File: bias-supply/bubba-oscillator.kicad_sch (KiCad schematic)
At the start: 14 parts, among them U1 MAX44243ASD+

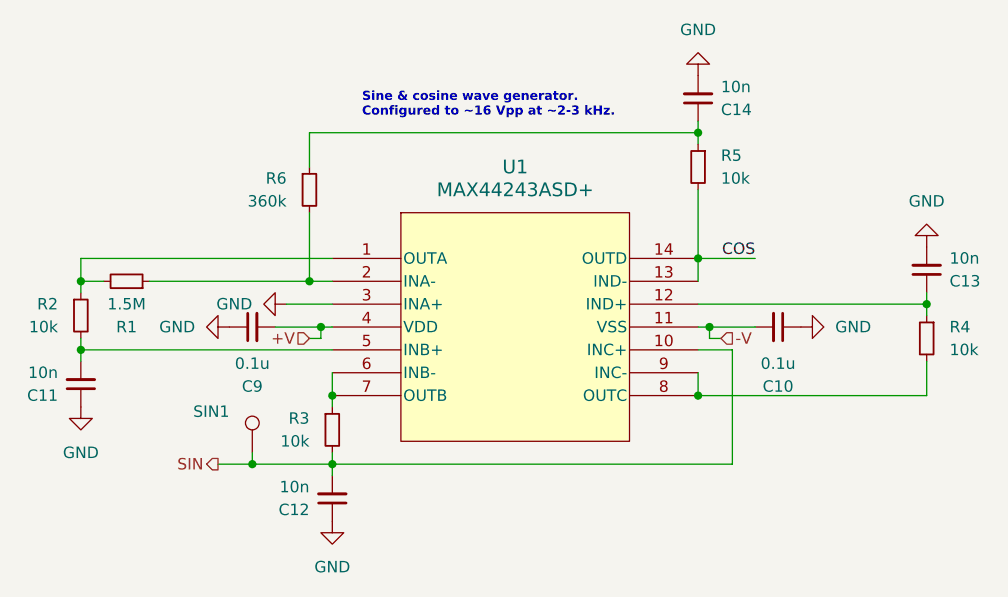
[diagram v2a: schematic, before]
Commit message: Add fuses; change to coax; fixed I2C gnd
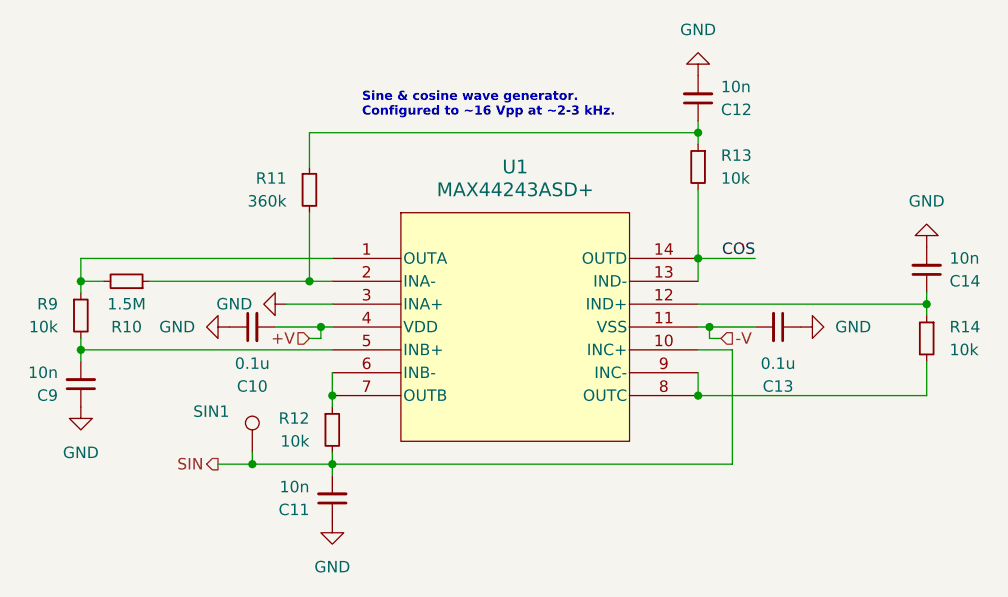
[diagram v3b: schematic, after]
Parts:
- renumbered C9 to C10, C12 to C11, C14 to C12, C10 to C13, C13 to C14, C11 to C9, R1 to R10, R6 to R11, R3 to R12, R5 to R13, R4 to R14, R2 to R9
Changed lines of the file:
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@@
 		(on_board yes)
 		(dnp no)
-		(property "Reference" "C14"
+		(property "Reference" "C12"
 			(at 171.45 63.4937 0)
 			(effects
@@
 			(project "bias-supply"
 				(path "/f3205b63-fc57-4ea3-95d4-2a447f249c30/9252fc98-7cb3-4026-81a7-b0bc1875cc02"
-					(reference "C14")
+					(reference "C12")
 					(unit 1)
 				)
@@
 		(on_board yes)
 		(dnp no)
-		(property "Reference" "C10"
+		(property "Reference" "C13"
 			(at 177.8 94.234 90)
 			(effects
@@
 			(project "bias-supply"
 				(path "/f3205b63-fc57-4ea3-95d4-2a447f249c30/9252fc98-7cb3-4026-81a7-b0bc1875cc02"
-					(reference "C10")
+					(reference "C13")
 					(unit 1)
 				)
@@
 		(dnp no)
 		(fields_autoplaced yes)
-		(property "Reference" "#PWR07"
+		(property "Reference" "#PWR08"
 			(at 100.33 102.87 0)
 			(effects
@@
 			(project "bias-supply"
 				(path "/f3205b63-fc57-4ea3-95d4-2a447f249c30/9252fc98-7cb3-4026-81a7-b0bc1875cc02"
-					(reference "#PWR07")
+					(reference "#PWR08")
 					(unit 1)
 				)
@@
 		(on_board yes)
 		(dnp no)
-		(property "Reference" "#PWR02"
+		(property "Reference" "#PWR010"
 			(at 116.84 85.09 0)
 			(effects
@@
 			(project "bias-supply"
 				(path "/f3205b63-fc57-4ea3-95d4-2a447f249c30/9252fc98-7cb3-4026-81a7-b0bc1875cc02"
-					(reference "#PWR02")
+					(reference "#PWR010")
 					(unit 1)
 				)
@@
 		(dnp no)
 		(fields_autoplaced yes)
-		(property "Reference" "#PWR010"
+		(property "Reference" "#PWR012"
 			(at 168.91 53.34 0)
 			(effects
@@
 			(project "bias-supply"
 				(path "/f3205b63-fc57-4ea3-95d4-2a447f249c30/9252fc98-7cb3-4026-81a7-b0bc1875cc02"
-					(reference "#PWR010")
+					(reference "#PWR012")
 					(unit 1)
 				)
@@
 		(on_board yes)
 		(dnp no)
-		(property "Reference" "C11"
+		(property "Reference" "C9"
 			(at 97.79 95.2437 0)
 			(effects
@@
 			(project "bias-supply"
 				(path "/f3205b63-fc57-4ea3-95d4-2a447f249c30/9252fc98-7cb3-4026-81a7-b0bc1875cc02"
-					(reference "C11")
+					(reference "C9")
 					(unit 1)
 				)
@@
 		(on_board yes)
 		(dnp no)
-		(property "Reference" "R1"
+		(property "Reference" "R10"
 			(at 105.41 87.63 90)
 			(effects
@@
 			(project ""
 				(path "/f3205b63-fc57-4ea3-95d4-2a447f249c30/9252fc98-7cb3-4026-81a7-b0bc1875cc02"
-					(reference "R1")
+					(reference "R10")
 					(unit 1)
 				)
@@
 		(dnp no)
 		(fields_autoplaced yes)
-		(property "Reference" "#PWR09"
+		(property "Reference" "#PWR014"
 			(at 194.31 72.39 0)
 			(effects
@@
 			(project "bias-supply"
 				(path "/f3205b63-fc57-4ea3-95d4-2a447f249c30/9252fc98-7cb3-4026-81a7-b0bc1875cc02"
-					(reference "#PWR09")
+					(reference "#PWR014")
 					(unit 1)
 				)
@@
 		(on_board yes)
 		(dnp no)
-		(property "Reference" "R5"
+		(property "Reference" "R13"
 			(at 171.45 68.5799 0)
 			(effects
@@
 			(project "bias-supply"
 				(path "/f3205b63-fc57-4ea3-95d4-2a447f249c30/9252fc98-7cb3-4026-81a7-b0bc1875cc02"
-					(reference "R5")
+					(reference "R13")
 					(unit 1)
 				)
@@
 		(on_board yes)
 		(dnp no)
-		(property "Reference" "C9"
+		(property "Reference" "C10"
 			(at 119.38 94.234 90)
 			(effects
@@
 			(project "bias-supply"
 				(path "/f3205b63-fc57-4ea3-95d4-2a447f249c30/9252fc98-7cb3-4026-81a7-b0bc1875cc02"
-					(reference "C9")
+					(reference "C10")
 					(unit 1)
 				)
@@
 		(on_board yes)
 		(dnp no)
-		(property "Reference" "R6"
+		(property "Reference" "R11"
 			(at 123.19 71.1199 0)
 			(effects
@@
 			(project "bias-supply"
 				(path "/f3205b63-fc57-4ea3-95d4-2a447f249c30/9252fc98-7cb3-4026-81a7-b0bc1875cc02"
-					(reference "R6")
+					(reference "R11")
 					(unit 1)
 				)
@@
 		(on_board yes)
 		(dnp no)
-		(property "Reference" "#PWR031"
+		(property "Reference" "#PWR013"
 			(at 186.69 87.63 0)
 			(effects
@@
 			(project "bias-supply"
 				(path "/f3205b63-fc57-4ea3-95d4-2a447f249c30/9252fc98-7cb3-4026-81a7-b0bc1875cc02"
-					(reference "#PWR031")
+					(reference "#PWR013")
 					(unit 1)
 				)
@@
 		(on_board yes)
 		(dnp no)
-		(property "Reference" "#PWR030"
+		(property "Reference" "#PWR09"
 			(at 110.49 87.63 0)
 			(effects
@@
 			(project "bias-supply"
 				(path "/f3205b63-fc57-4ea3-95d4-2a447f249c30/9252fc98-7cb3-4026-81a7-b0bc1875cc02"
-					(reference "#PWR030")
+					(reference "#PWR09")
 					(unit 1)
 				)
@@
 		(on_board yes)
 		(dnp no)
-		(property "Reference" "R2"
+		(property "Reference" "R9"
 			(at 97.79 85.0899 0)
 			(effects
@@
 			(project ""
 				(path "/f3205b63-fc57-4ea3-95d4-2a447f249c30/9252fc98-7cb3-4026-81a7-b0bc1875cc02"
-					(reference "R2")
+					(reference "R9")
 					(unit 1)
 				)
@@
 		(on_board yes)
 		(dnp no)
-		(property "Reference" "C12"
+		(property "Reference" "C11"
 			(at 125.73 107.9437 0)
 			(effects
@@
 			(project "bias-supply"
 				(path "/f3205b63-fc57-4ea3-95d4-2a447f249c30/9252fc98-7cb3-4026-81a7-b0bc1875cc02"
-					(reference "C12")
+					(reference "C11")
 					(unit 1)
 				)
@@
 		(on_board yes)
 		(dnp no)
-		(property "Reference" "#PWR08"
+		(property "Reference" "#PWR011"
 			(at 128.27 115.57 0)
 			(effects
@@
 			(project "bias-supply"
 				(path "/f3205b63-fc57-4ea3-95d4-2a447f249c30/9252fc98-7cb3-4026-81a7-b0bc1875cc02"
-					(reference "#PWR08")
+					(reference "#PWR011")
 					(unit 1)
 				)
@@
 		(on_board yes)
 		(dnp no)
-		(property "Reference" "C13"
+		(property "Reference" "C14"
 			(at 196.85 82.5437 0)
 			(effects
@@
 			(project "bias-supply"
 				(path "/f3205b63-fc57-4ea3-95d4-2a447f249c30/9252fc98-7cb3-4026-81a7-b0bc1875cc02"
-					(reference "C13")
+					(reference "C14")
 					(unit 1)
 				)
@@
 		(on_board yes)
 		(dnp no)
-		(property "Reference" "R4"
+		(property "Reference" "R14"
 			(at 196.85 87.6299 0)
 			(effects
@@
 			(project "bias-supply"
 				(path "/f3205b63-fc57-4ea3-95d4-2a447f249c30/9252fc98-7cb3-4026-81a7-b0bc1875cc02"
-					(reference "R4")
+					(reference "R14")
 					(unit 1)
 				)
@@
 		(on_board yes)
 		(dnp no)
-		(property "Reference" "R3"
+		(property "Reference" "R12"
 			(at 125.73 97.7899 0)
 			(effects
@@
 			(project "bias-supply"
 				(path "/f3205b63-fc57-4ea3-95d4-2a447f249c30/9252fc98-7cb3-4026-81a7-b0bc1875cc02"
-					(reference "R3")
-					(unit 1)
-				)
+					(reference "R12")
+					(unit 1)
+				)

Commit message: Bubba V2.1
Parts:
- SIN1: now left out of the parts list
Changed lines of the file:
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@@
 	(title_block
 		(title "Bubba oscillator")
-		(date "2025-06-12")
-		(rev "2.0")
+		(date "2026-03-05")
+		(rev "2.1")
 	)
 	(text "Sine & cosine wave generator.\nConfigured to ~16 Vpp at ~2-3 kHz."
@@
 		(unit 1)
 		(exclude_from_sim no)
-		(in_bom yes)
+		(in_bom no)
 		(on_board yes)
 		(dnp no)
@@
 			)
 		)
-		(property "Datasheet" "~"
+		(property "Datasheet" "https://search.murata.co.jp/Ceramy/image/img/A01X/G101/ENG/GCM3195C2A103GA16-01A.pdf"
 			(at 168.91 62.23 0)
 			(effects
@@
 			)
 		)
-		(property "Description" ""
+		(property "Description" "GCM3195C2A103GA16D"
 			(at 168.91 62.23 0)
 			(effects
@@
 			)
 		)
-		(property "Datasheet" "~"
+		(property "Datasheet" "https://search.murata.co.jp/Ceramy/image/img/A01X/G101/ENG/GRM3195C2A104GA01-01A.pdf"
 			(at 177.8 87.63 0)
 			(effects
@@
 			)
 		)
-		(property "Description" "Unpolarized capacitor, small symbol"
+		(property "Description" "GRM3195C2A104GA01D"
 			(at 177.8 87.63 0)
 			(effects
@@
 			)
 		)
-		(property "Datasheet" "~"
+		(property "Datasheet" "https://search.murata.co.jp/Ceramy/image/img/A01X/G101/ENG/GCM3195C2A103GA16-01A.pdf"
 			(at 100.33 93.98 0)
 			(effects
@@
 			)
 		)
-		(property "Description" ""
+		(property "Description" "GCM3195C2A103GA16D"
 			(at 100.33 93.98 0)
 			(effects
@@
 			)
 		)
-		(property "Datasheet" "~"
+		(property "Datasheet" "https://www.seielect.com/catalog/SEI-RMCF_RMCP.pdf"
 			(at 105.41 82.55 0)
 			(effects
@@
 			)
 		)
-		(property "Description" "Resistor, small symbol"
+		(property "Description" "RMCF1206FT1M50"
 			(at 105.41 82.55 0)
 			(effects
@@
 			)
 		)
-		(property "Description" ""
+		(property "Description" "MAX44243ASD+"
 			(at 128.27 80.01 0)
 			(effects
@@
 			)
 		)
-		(property "Datasheet" "~"
+		(property "Datasheet" "https://yageogroup.com/content/datasheet/asset/file/PYU-RC_GROUP_51_ROHS_L"
 			(at 168.91 69.85 0)
 			(effects
@@
 			)
 		)
-		(property "Description" "Resistor, small symbol"
+		(property "Description" "RC1206FR-0710KL"
 			(at 168.91 69.85 0)
 			(effects
@@
 			)
 		)
-		(property "Datasheet" "~"
+		(property "Datasheet" "https://search.murata.co.jp/Ceramy/image/img/A01X/G101/ENG/GRM3195C2A104GA01-01A.pdf"
 			(at 119.38 87.63 0)
 			(effects
@@
 			)
 		)
-		(property "Description" "Unpolarized capacitor, small symbol"
+		(property "Description" "GRM3195C2A104GA01D"
 			(at 119.38 87.63 0)
 			(effects
@@
 			)
 		)
-		(property "Datasheet" "~"
+		(property "Datasheet" "https://yageogroup.com/content/datasheet/asset/file/PYU-RC_GROUP_51_ROHS_L"
 			(at 125.73 72.39 0)
 			(effects
@@
 			)
 		)
-		(property "Description" "Resistor, small symbol"
+		(property "Description" "RC1206FR-07360KL"
 			(at 125.73 72.39 0)
 			(effects
@@
 			)
 		)
-		(property "Datasheet" "~"
+		(property "Datasheet" "https://yageogroup.com/content/datasheet/asset/file/PYU-RC_GROUP_51_ROHS_L"
 			(at 100.33 86.36 0)
 			(effects
@@
 			)
 		)
-		(property "Description" "Resistor, small symbol"
+		(property "Description" "RC1206FR-0710KL"
 			(at 100.33 86.36 0)
 			(effects
@@
 			)
 		)
-		(property "Datasheet" "~"
+		(property "Datasheet" "https://search.murata.co.jp/Ceramy/image/img/A01X/G101/ENG/GCM3195C2A103GA16-01A.pdf"
 			(at 128.27 106.68 0)
 			(effects
@@
 			)
 		)
-		(property "Description" ""
+		(property "Description" "GCM3195C2A103GA16D"
 			(at 128.27 106.68 0)
 			(effects
@@
 			)
 		)
-		(property "Datasheet" "~"
+		(property "Datasheet" "https://search.murata.co.jp/Ceramy/image/img/A01X/G101/ENG/GCM3195C2A103GA16-01A.pdf"
 			(at 194.31 81.28 0)
 			(effects
@@
 			)
 		)
-		(property "Description" ""
+		(property "Description" "GCM3195C2A103GA16D"
 			(at 194.31 81.28 0)
 			(effects
@@
 			)
 		)
-		(property "Datasheet" "~"
+		(property "Datasheet" "https://yageogroup.com/content/datasheet/asset/file/PYU-RC_GROUP_51_ROHS_L"
 			(at 194.31 88.9 0)
 			(effects
@@
 			)
 		)
-		(property "Description" "Resistor, small symbol"
+		(property "Description" "RC1206FR-0710KL"
 			(at 194.31 88.9 0)
 			(effects
@@
 			)
 		)
-		(property "Datasheet" "~"
+		(property "Datasheet" "https://yageogroup.com/content/datasheet/asset/file/PYU-RC_GROUP_51_ROHS_L"
 			(at 128.27 99.06 0)
 			(effects
@@
 			)
 		)
-		(property "Description" "Resistor, small symbol"
+		(property "Description" "RC1206FR-0710KL"
 			(at 128.27 99.06 0)
 			(effects
